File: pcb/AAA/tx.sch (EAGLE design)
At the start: 52 parts, among them U3 MCP73831T-2ACI/OT, Y1 CRYSTAL-26MHZSMD-3.2X2.5

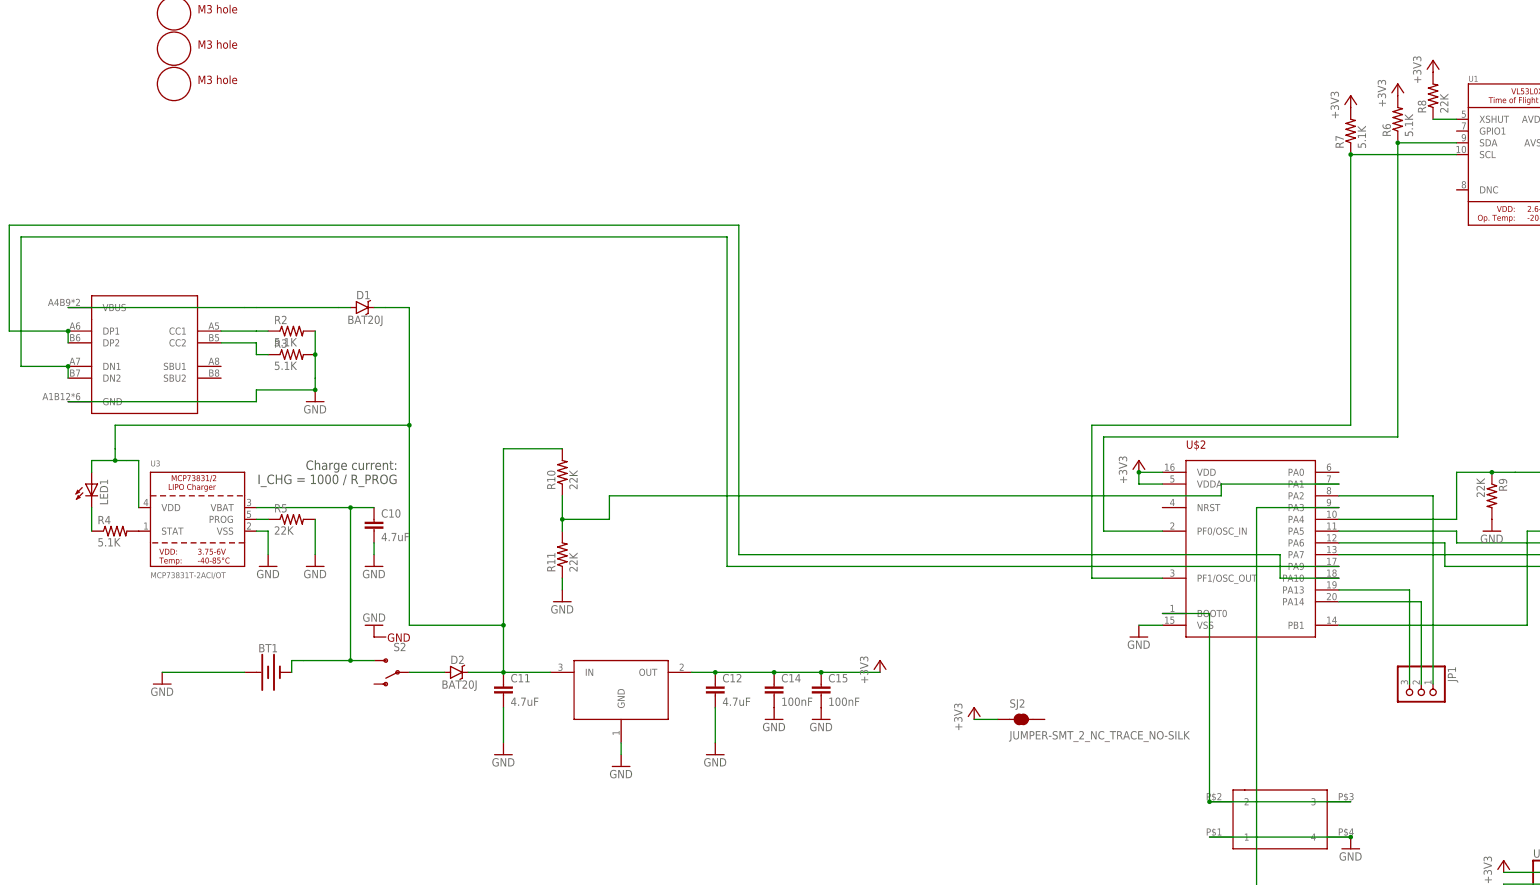
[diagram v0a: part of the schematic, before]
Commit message: usb on tx
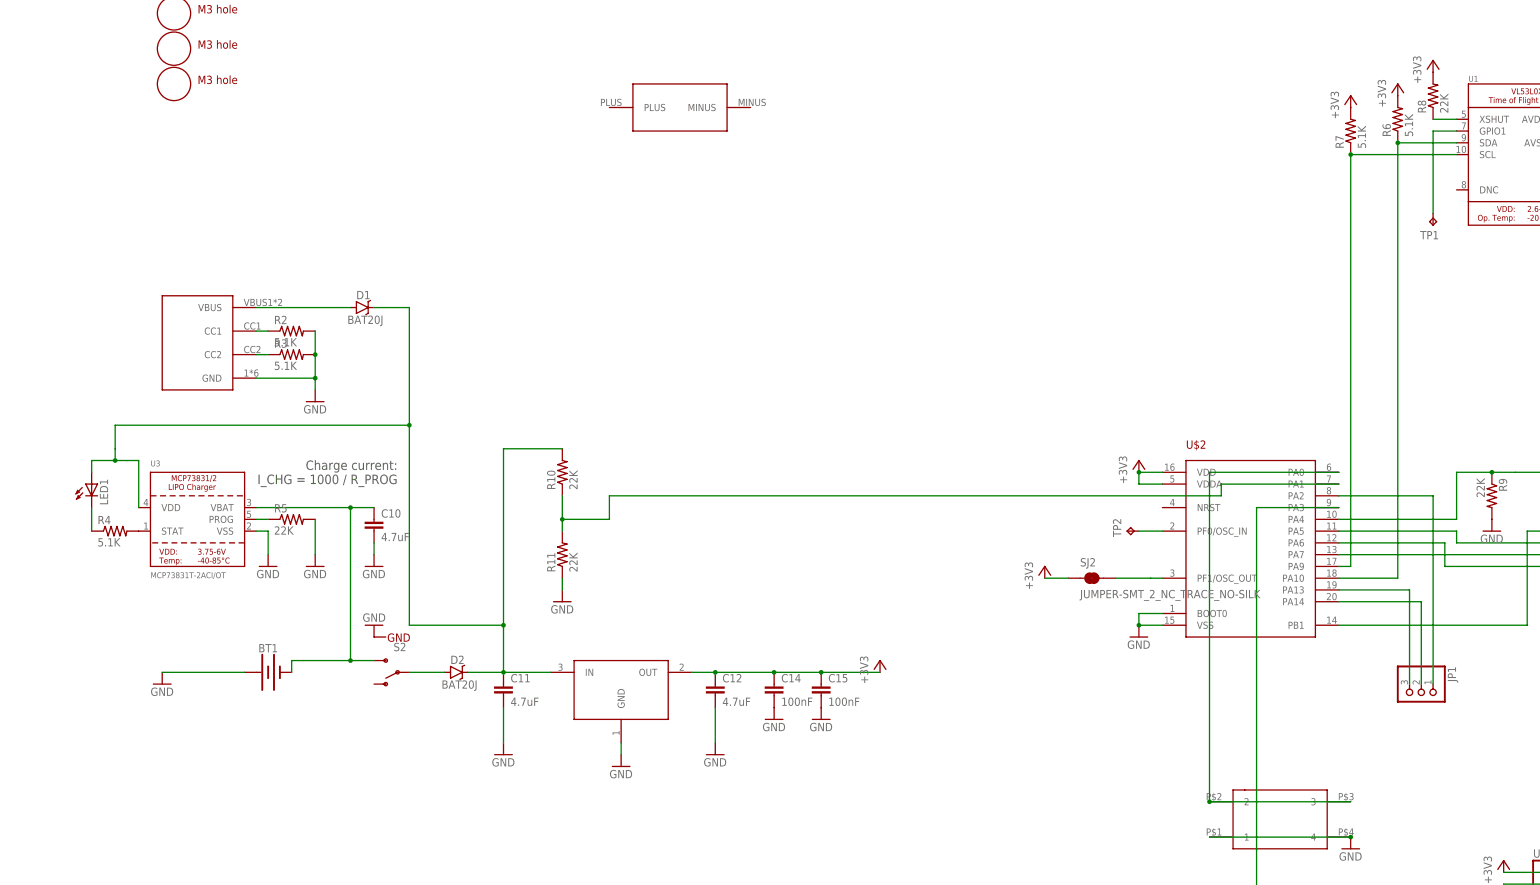
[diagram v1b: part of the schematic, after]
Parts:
- added TP1, TP2: TPTP12R, testpad:TPTP12R
- added U$1: L1_USBC_6P_DEV, tx:L1_USBC_6P_DEV
- U$4: value USBC_16P -> AAA_SYM; device my_usbc_16p:USBC_16P -> 3pos_slide_switch:AAA_SYM
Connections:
- removed net N$23: R6.1, U$2.PF0/OSC_IN, U1.SDA
- new net N$36: TP1.TP, U1.GPIO1
- new net N$37: TP2.TP, U$2.PF0/OSC_IN
- net GND: now also U$1.GND, U$2.BOOT0; no longer U$4.GND
- net N$10: now also U$1.CC2; no longer U$4.CC2
- net N$11: now also U$1.CC1; no longer U$4.CC1
- net N$18: now also R6.1, U1.SDA; no longer U$4.DP1, U$4.DP2
- net N$22: now also U$2.PA9; no longer U$2.PF1/OSC_OUT
- net N$26: now also U$1.VBUS; no longer U$4.VBUS
- net N$30: now also U$2.PA0; no longer U$2.BOOT0
- net N$34: now also SJ2.2, U$2.PF1/OSC_OUT; no longer U$2.PA9, U$4.DN1, U$4.DN2
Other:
- moved on the sheet: SJ2
